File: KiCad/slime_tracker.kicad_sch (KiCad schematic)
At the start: 51 parts, among them J1 batt, J2 Extension, J3 USB_C_Receptacle_PowerOnly_6P, SW1 SW_DPDT_x2, U1 TP4056, U3 TPS7A0333PDBVR, U4 ESP32 SUPER MINI C3, U5 TPS61090

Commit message: REV0.3
REV 0.3

TVS, EN/CE Based control, SPI I2C selectable Footprint, ESP32 Footprint changed,  etc
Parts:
- removed FB1: FerriteBead, Resistor_SMD:R_0805_2012Metric, symbol Device:FerriteBead
- added D4: D_TVS, Diode_SMD:D_SOD-323, symbol Device:D_TVS
- added R20: 0Ω, Resistor_SMD:R_0603_1608Metric, symbol Device:R
- added R21, R22: 100kΩ, Resistor_SMD:R_0603_1608Metric, symbol Device:R
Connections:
- net 3v3: now also U3.5 (OUT), R20.1
- net AGND: now also D4.2 (A2), R21.2, R22.2
- net BAT+: now also C12.1, C2.2, L1.1, R1.1, U1.5 (BAT), U5.8 (VBAT), D4.1 (A1)
- net BAT-_TO_BOOST: now also R22.1; no longer C2.2, L1.1, R1.1, U5.8 (VBAT)
- net BAT-_TO_CHG: now also U1.8 (CE), R21.1; no longer C12.1, U1.5 (BAT)
- net MISO: now also R20.2
- net at C13.1, D1.2 (A), D2.2 (A)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: no longer U1.8 (CE)
- no-connect marks 2 -> 18
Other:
- note added: "PESD5V0S1BA"
- note removed: "BEAD SIZE 0805"
- moved on the sheet: C1, C10, C11, C12, C13, C3, C4, C6, C7, D1, D2, D3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

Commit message: REV3 TD
TeadDrop
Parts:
- C8: footprint Capacitor_Tantalum_SMD:CP_EIA-7343-20_Kemet-V -> Capacitor_Tantalum_SMD:CP_EIA-7343-31_Kemet-D
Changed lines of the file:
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@@
 			)
 		)
-		(property "Footprint" "Capacitor_Tantalum_SMD:CP_EIA-7343-20_Kemet-V"
+		(property "Footprint" "Capacitor_Tantalum_SMD:CP_EIA-7343-31_Kemet-D"
 			(at 127.9652 40.64 0)
 			(effects

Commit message: REV_03
LC filter damp R added
USB Vbus TVS added
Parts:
- added D5: D_TVS, Diode_SMD:D_SOD-323, symbol Device:D_TVS
- added R23, R24: 1Ω, Resistor_SMD:R_1206_3216Metric, symbol Device:R
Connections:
- net 5V: now also R23.1, R24.1; no longer C10.2
- net AGND: now also D5.2 (A2)
- net C-TYPE+: now also D5.1 (A1)
- new net: C10.2, R23.2, R24.2
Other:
- moved on the sheet: C10, L2

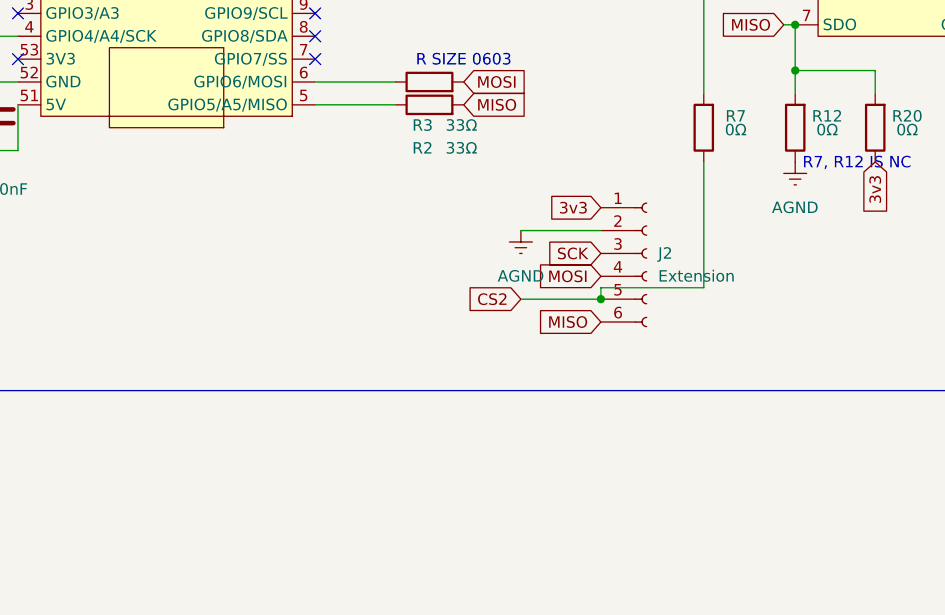
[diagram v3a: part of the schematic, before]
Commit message: Rev 03 more TVS
more TVS at extend port line
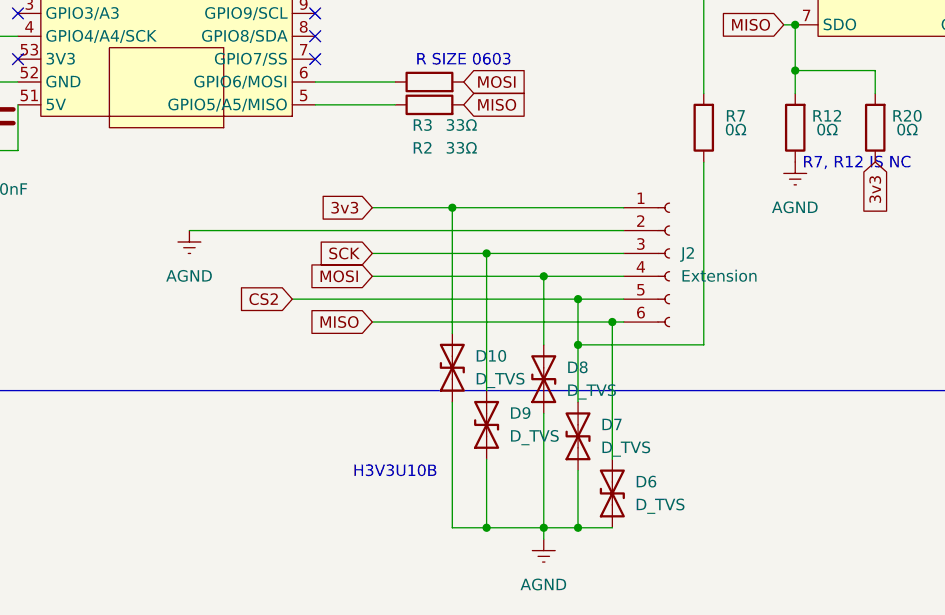
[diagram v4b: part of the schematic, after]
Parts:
- added D10, D6, D7, D8, D9: D_TVS, slime:DFN1006-2, symbol Device:D_TVS
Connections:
- net 3v3: now also D10.2 (A2)
- net AGND: now also D10.1 (A1), D6.1 (A1), D7.1 (A1), D8.1 (A1), D9.1 (A1)
- net CS2: now also D7.2 (A2)
- net MISO: now also D6.2 (A2)
- net MOSI: now also D8.2 (A2)
- net SCK: now also D9.2 (A2)
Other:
- note added: "H3V3U10B"
- moved on the sheet: J2

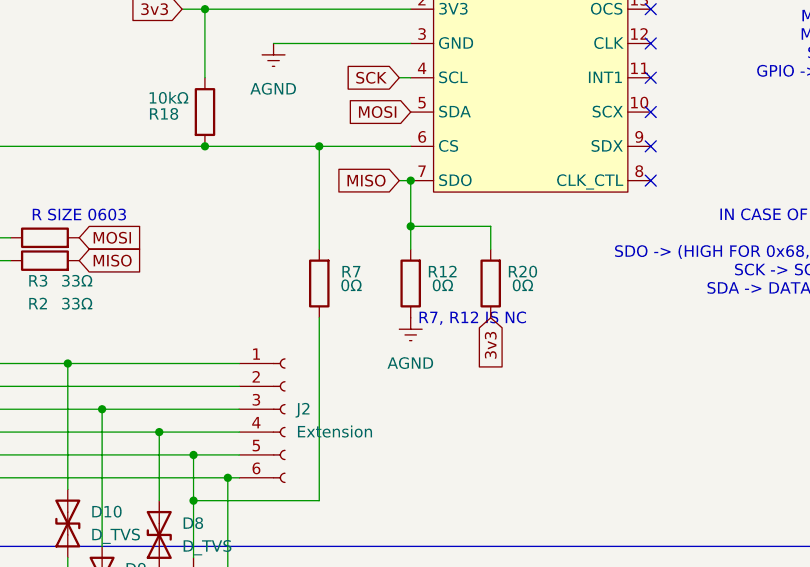
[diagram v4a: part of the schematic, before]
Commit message: REV03 3/11
few PCB layout changed
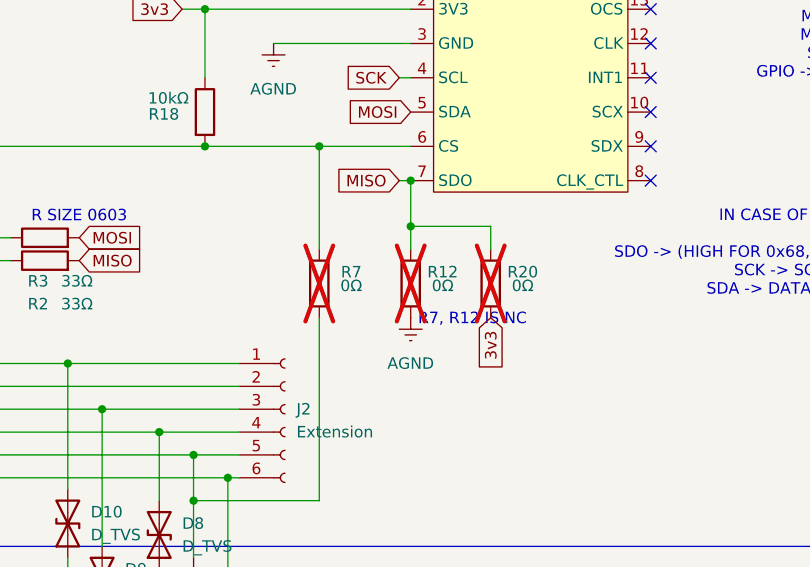
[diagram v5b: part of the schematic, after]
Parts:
- R12, R20, R7: now not fitted
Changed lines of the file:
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@@
 		(in_bom yes)
 		(on_board yes)
-		(dnp no)
+		(dnp yes)
 		(property "Reference" "R7"
 			(at 335.026 153.67 0)
@@
 		(in_bom yes)
 		(on_board yes)
-		(dnp no)
+		(dnp yes)
 		(property "Reference" "R12"
 			(at 345.186 153.67 0)
@@
 		(in_bom yes)
 		(on_board yes)
-		(dnp no)
+		(dnp yes)
 		(property "Reference" "R20"
 			(at 354.076 153.67 0)

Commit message: rev03 agnd pgnd
agnd pgnd
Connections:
- net AGND: now also U4.0 (GPIO0/A0), U4.2 (GPIO2/A2), U4.3 (GPIO3/A3), U4.53 (3V3), U4.7 (GPIO7/SS)
- no-connect marks 18 -> 13
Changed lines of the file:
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@@
 	)
 	(junction
+		(at 254 125.73)
+		(diameter 0)
+		(color 0 0 0 0)
+	)
+	(junction
 		(at 172.72 96.52)
 		(diameter 0)
@@
 	)
 	(junction
+		(at 254 134.62)
+		(diameter 0)
+		(color 0 0 0 0)
+	)
+	(junction
 		(at 68.58 133.35)
 		(diameter 0)
@@
 	)
 	(junction
+		(at 254 139.7)
+		(diameter 0)
+		(color 0 0 0 0)
+	)
+	(junction
 		(at 317.5 173.99)
 		(diameter 0)
@@
 	)
 	(junction
+		(at 254 142.24)
+		(diameter 0)
+		(color 0 0 0 0)
+	)
+	(junction
 		(at 307.34 168.91)
 		(diameter 0)
@@
 	)
 	(no_connect
-		(at 255.27 134.62)
-	)
-	(no_connect
 		(at 288.29 142.24)
 	)
 	(no_connect
-		(at 255.27 147.32)
-	)
-	(no_connect
-		(at 255.27 142.24)
-	)
-	(no_connect
 		(at 368.3 124.46)
 	)
@@
 	)
 	(no_connect
-		(at 288.29 147.32)
-	)
-	(no_connect
 		(at 288.29 134.62)
 	)
@@
 		(at 341.63 120.65)
 	)
-	(no_connect
-		(at 255.27 139.7)
-	)
 	(wire
 		(pts
@@
 	(wire
 		(pts
+			(xy 254 134.62) (xy 255.27 134.62)
+		)
+		(stroke
+			(width 0)
+			(type default)
+		)
+	)
+	(wire
+		(pts
 			(xy 318.77 139.7) (xy 331.47 139.7)
 		)
@@
 	(wire
 		(pts
+			(xy 295.91 147.32) (xy 295.91 125.73)
+		)
+		(stroke
+			(width 0)
+			(type default)
+		)
+	)
+	(wire
+		(pts
 			(xy 294.64 85.09) (xy 290.83 85.09)
 		)
@@
 	(wire
 		(pts
+			(xy 254 142.24) (xy 254 139.7)
+		)
+		(stroke
+			(width 0)
+			(type default)
+		)
+	)
+	(wire
+		(pts
 			(xy 285.75 173.99) (xy 317.5 173.99)
 		)
@@
 		)
 	)
+	(wire
+		(pts
+			(xy 254 125.73) (xy 254 134.62)
+		)
+		(stroke
+			(width 0)
+			(type default)
+		)
+	)
 	(polyline
 		(pts
@@
 	(wire
 		(pts
+			(xy 254 134.62) (xy 254 139.7)
+		)
+		(stroke
+			(width 0)
+			(type default)
+		)
+	)
+	(wire
+		(pts
 			(xy 125.73 138.43) (xy 125.73 149.86)
 		)
@@
 		)
 	)
+	(wire
+		(pts
+			(xy 295.91 125.73) (xy 254 125.73)
+		)
+		(stroke
+			(width 0)
+			(type default)
+		)
+	)
 	(polyline
 		(pts
@@
 	(wire
 		(pts
+			(xy 255.27 139.7) (xy 254 139.7)
+		)
+		(stroke
+			(width 0)
+			(type default)
+		)
+	)
+	(wire
+		(pts
 			(xy 115.57 43.18) (xy 115.57 40.64)
 		)
@@
 	(wire
 		(pts
+			(xy 255.27 147.32) (xy 254 147.32)
+		)
+		(stroke
+			(width 0)
+			(type default)
+		)
+	)
+	(wire
+		(pts
 			(xy 96.52 45.72) (xy 96.52 52.07)
 		)
@@
 	(wire
 		(pts
+			(xy 254 147.32) (xy 254 142.24)
+		)
+		(stroke
+			(width 0)
+			(type default)
+		)
+	)
+	(wire
+		(pts
 			(xy 68.58 90.17) (xy 55.88 90.17)
 		)
@@
 	(wire
 		(pts
+			(xy 255.27 142.24) (xy 254 142.24)
+		)
+		(stroke
+			(width 0)
+			(type default)
+		)
+	)
+	(wire
+		(pts
 			(xy 237.49 101.6) (xy 232.41 101.6)
 		)
@@
 	(wire
 		(pts
+			(xy 288.29 147.32) (xy 295.91 147.32)
+		)
+		(stroke
+			(width 0)
+			(type default)
+		)
+	)
+	(wire
+		(pts
 			(xy 156.21 171.45) (xy 158.75 171.45)
 		)
@@
 					(unit 1)
 				)
+			)
+		)
+	)
+	(symbol
+		(lib_id "power:GNDREF")
+		(at 254 125.73 180)
+		(unit 1)
+		(exclude_from_sim no)
+		(in_bom yes)
+		(on_board yes)
+		(dnp no)
+		(fields_autoplaced yes)
+		(property "Reference" "#PWR026"
+			(at 254 119.38 0)
+			(effects
+				(font
+					(size 1.27 1.27)
+				)
+				(hide yes)
+			)
+		)
+		(property "Value" "AGND"
+			(at 254 120.65 0)
+			(effects
+				(font
+					(size 1.27 1.27)
+				)
+			)
+		)
+		(property "Footprint" ""
+			(at 254 125.73 0)
+			(effects
+				(font
+					(size 1.27 1.27)
+				)
+				(hide yes)
+			)
+		)
+		(property "Datasheet" ""
+			(at 254 125.73 0)
+			(effects
+				(font
+					(size 1.27 1.27)
+				)
+				(hide yes)
+			)
+		)
+		(property "Description" "Power symbol creates a global label with name \"GNDREF\" , reference supply ground"
+			(at 254 125.73 0)
+			(effects
+				(font
+					(size 1.27 1.27)
+				)
+				(hide yes)
+			)
+		)
+		(pin "1"
+		)
+		(instances
+			(project "slime_tracker"
+				(path "/9f3f9b38-d2e1-497f-9960-ea0c5443957e"
+					(reference "#PWR026")
+					(unit 1)
+				)

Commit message: LPF Changed
dd
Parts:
- added C16: 22uF, Capacitor_SMD:C_0805_2012Metric, symbol Device:C
- added C9: 4.7uF, Capacitor_SMD:C_0805_2012Metric, symbol Device:C
- C10: value 4.7uF -> 22uF; footprint Capacitor_SMD:C_1206_3216Metric -> Capacitor_SMD:C_0805_2012Metric
- C11, C4, C5: footprint Capacitor_SMD:C_1206_3216Metric -> Capacitor_SMD:C_0603_1608Metric
- C12, C13, C3: footprint Capacitor_SMD:C_1206_3216Metric -> Capacitor_SMD:C_0805_2012Metric
- C6, C7: footprint Capacitor_SMD:C_0805_2012Metric -> Capacitor_SMD:C_0603_1608Metric
- L2: value 2.2uH -> 3uH
- R23, R24: footprint Resistor_SMD:R_1206_3216Metric -> Resistor_SMD:R_0603_1608Metric
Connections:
- net 5V: now also C9.2
- net AGND: now also C16.1, C9.1
- net at C10.2, R23.2, R24.2: now also C16.2
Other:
- note added: "CAP SIZE 0603"
- note added: "CAP SIZE 0805 25V"
- note added: "Cd total 44uF SIZE 0805 Rd 0.5 SIZE 0603"
- note added: "FNR5020S3R0NT 3uH +-30%"
- note added: "T520D107M010ATE055"
- note removed: "FXL0420-2R2-M"
- note removed: "tantalum cap T520V107M010ATE050"
- moved on the sheet: C1, C6, L2

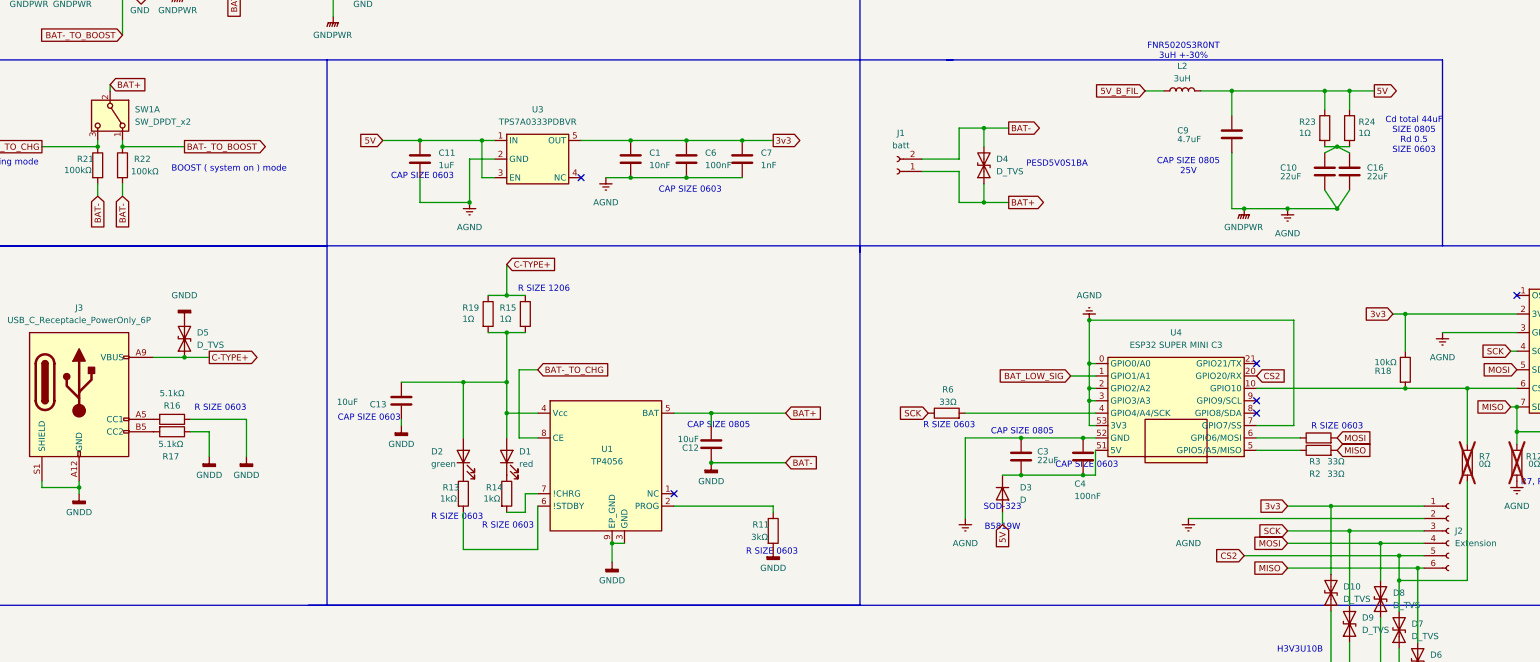
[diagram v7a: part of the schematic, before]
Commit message: 배치 안함
추가
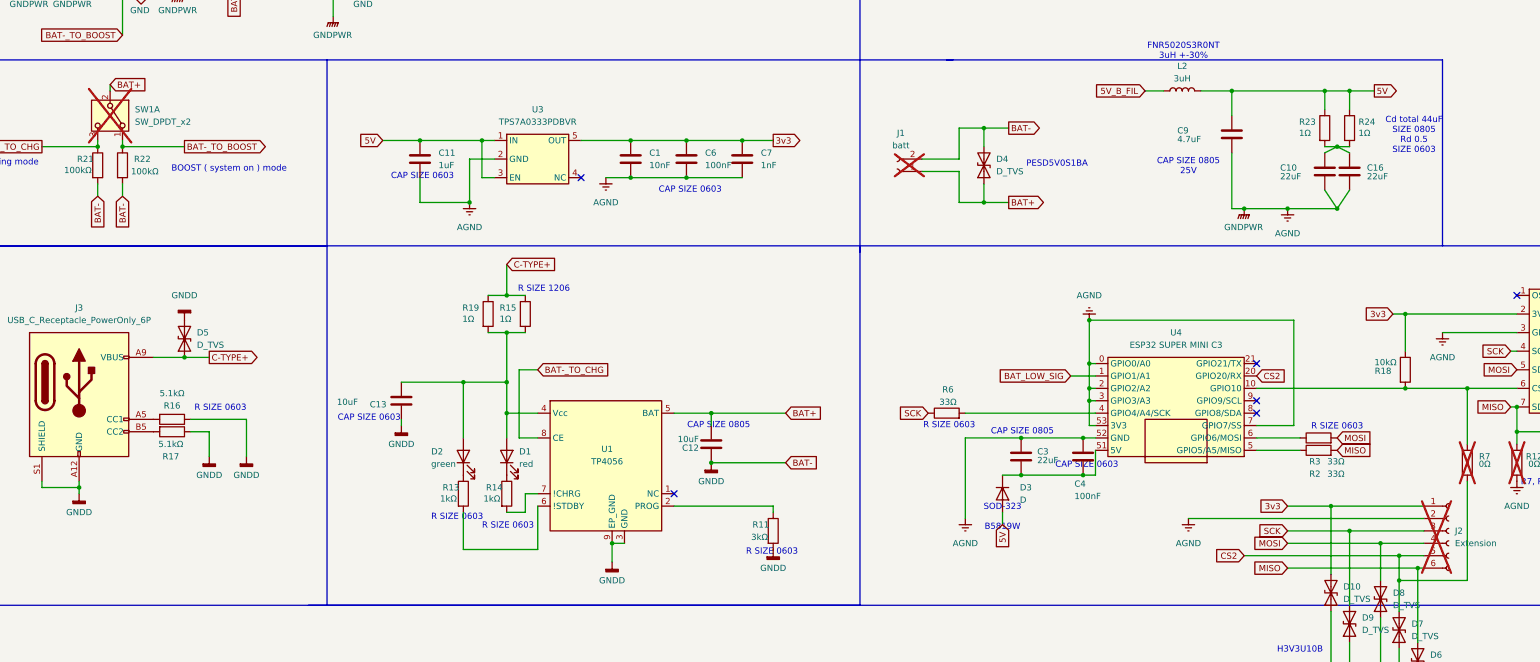
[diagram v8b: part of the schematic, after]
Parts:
- J1, SW1: now not fitted
- J2: now not fitted; now left out of the parts list
- L2: footprint slime:FXL0420 -> slime:FNR5020S3R0NT
- R12, R20, R7: now left out of the parts list
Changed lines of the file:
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@@
 		(unit 1)
 		(exclude_from_sim no)
-		(in_bom yes)
+		(in_bom no)
 		(on_board yes)
 		(dnp yes)
@@
 			)
 		)
-		(property "Footprint" "slime:FXL0420"
+		(property "Footprint" "slime:FNR5020S3R0NT"
 			(at 273.05 78.74 0)
 			(effects
@@
 		(in_bom no)
 		(on_board yes)
-		(dnp no)
+		(dnp yes)
 		(fields_autoplaced yes)
 		(property "Reference" "SW1"
@@
 		(unit 1)
 		(exclude_from_sim no)
-		(in_bom yes)
+		(in_bom no)
 		(on_board yes)
 		(dnp yes)
@@
 		(in_bom no)
 		(on_board yes)
-		(dnp no)
+		(dnp yes)
 		(property "Reference" "J1"
 			(at 215.392 87.376 0)
@@
 		(unit 1)
 		(exclude_from_sim no)
-		(in_bom yes)
+		(in_bom no)
 		(on_board yes)
 		(dnp yes)
@@
 		(unit 1)
 		(exclude_from_sim no)
-		(in_bom yes)
+		(in_bom no)
 		(on_board yes)
-		(dnp no)
+		(dnp yes)
 		(fields_autoplaced yes)
 		(property "Reference" "J2"
